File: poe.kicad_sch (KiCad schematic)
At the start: 85 parts

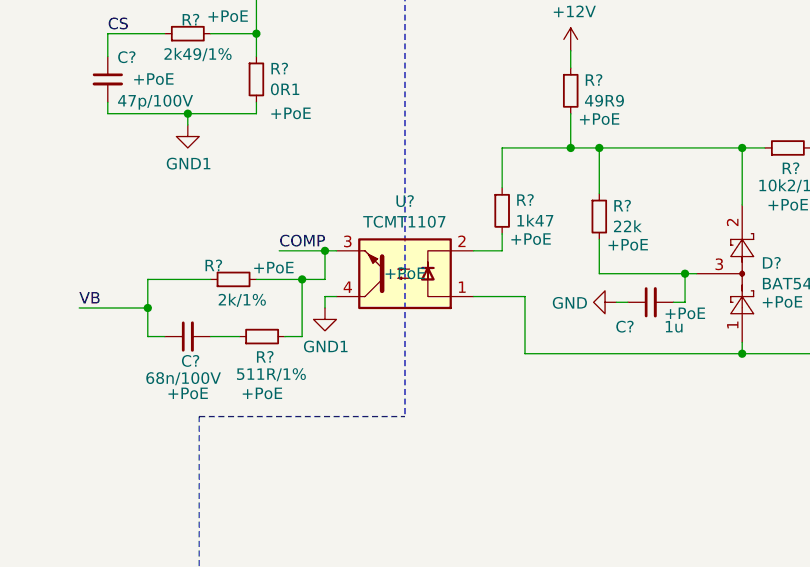
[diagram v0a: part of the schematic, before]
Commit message: poe.kicad_sch: Flip the optocoupler
Signed-off-by: Dominik Sliwa <dominik@sliwa.io>
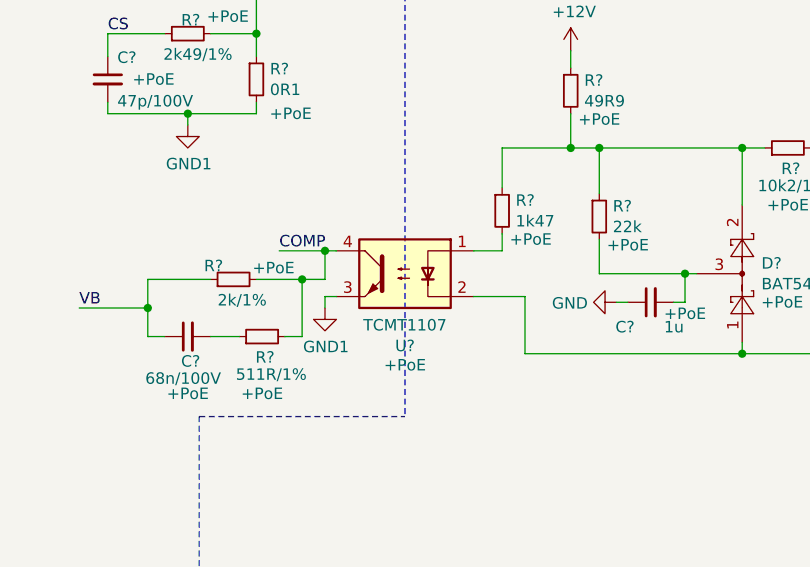
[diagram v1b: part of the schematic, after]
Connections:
- net COMP: now also U?.4; no longer U?.3
- net GND1: now also U?.3; no longer U?.4
- net at C?.2, D?.1, R?.2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: now also U?.2; no longer U?.1
- net at R?.2: now also U?.1; no longer U?.2
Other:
- moved on the sheet: U?
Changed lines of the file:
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@@
   (junction (at 274.32 35.56) (diameter 0.9144) (color 0 0 0 0))
   (junction (at 281.94 139.065) (diameter 0.9144) (color 0 0 0 0))
+  (no_connect (at 113.03 129.54))
+  (no_connect (at 72.39 157.48))
   (no_connect (at 72.39 129.54))
   (no_connect (at 72.39 154.94))
-  (no_connect (at 72.39 157.48))
-  (no_connect (at 113.03 129.54))
   (bus_entry (at 33.02 33.02) (size 2.54 2.54)
     (stroke (width 0.1524) (type solid) (color 0 0 0 0))
@@
     (property "Config" "+PoE" (id 4) (at 241.3 152.4 90))
   )
-  (symbol (lib_id "Isolator:TCMT1107") (at 199.39 149.225 180) (unit 1)
-    (in_bom yes) (on_board yes)
-    (property "Reference" "U?" (id 0) (at 199.39 141.2048 0))
-    (property "Value" "TCMT1107" (id 1) (at 199.39 143.5035 0))
-    (property "Footprint" "Package_SO:SOP-4_4.4x2.6mm_P1.27mm" (id 2) (at 199.39 141.605 0)
-      (effects (font (size 1.27 1.27)) hide)
-    )
-    (property "Datasheet" "http://www.vishay.com/docs/83510/tcmt1100.pdf" (id 3) (at 199.39 147.955 0)
+  (symbol (lib_id "Isolator:TCMT1107") (at 199.39 149.225 0) (mirror y) (unit 1)
+    (in_bom yes) (on_board yes)
+    (property "Reference" "U?" (id 0) (at 199.39 157.2452 0))
+    (property "Value" "TCMT1107" (id 1) (at 199.39 154.9465 0))
+    (property "Footprint" "Package_SO:SOP-4_4.4x2.6mm_P1.27mm" (id 2) (at 199.39 156.845 0)
+      (effects (font (size 1.27 1.27)) hide)
+    )
+    (property "Datasheet" "http://www.vishay.com/docs/83510/tcmt1100.pdf" (id 3) (at 199.39 150.495 0)
       (effects (font (size 1.27 1.27)) (justify left) hide)
     )
-    (property "Config" "+PoE" (id 4) (at 199.39 149.225 0))
+    (property "Config" "+PoE" (id 4) (at 199.39 159.385 0))
   )
   (symbol (lib_id "LightBlue:Transformer_Wurth_749119550") (at 199.39 45.72 0) (unit 1)

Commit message: Annotate symbools and assign capacitor footprints
Signed-off-by: Stefan Agner <stefan@agner.ch>
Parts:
- C70, C71, C72, C73, C74, C75, C76, C77, C78, C79, C80, C81, C82, C83, C84, C85, C86: renamed from C?; footprint (none) -> Capacitor_SMD:C_0805_2012Metric
- C87, C88, C89, C90, C91: renamed from C?; footprint (none) -> Capacitor_SMD:C_0402_1005Metric
- C92, C93: renamed from C?; footprint (none) -> Capacitor_Tantalum_SMD:CP_EIA-7343-31_Kemet-D
- gave numbers to parts that had none: 61

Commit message: Standardize page settings/add page titles
Signed-off-by: Stefan Agner <stefan@agner.ch>
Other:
- company: (none) -> Nabu Casa
- title: (none) -> Power over Ethernet
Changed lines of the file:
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@@
 (kicad_sch (version 20201015) (generator eeschema)
   (paper "A4")
+  (title_block
+    (title "Power over Ethernet")
+    (date "2021-01-12")
+    (rev "0.1")
+    (company "Nabu Casa")
+    (comment 1 "www.nabucasa.com")
+    (comment 2 "Light Blue")
+  )
   (junction (at 38.735 109.22) (diameter 0.9144) (color 0 0 0 0))
   (junction (at 40.64 35.56) (diameter 0.9144) (color 0 0 0 0))

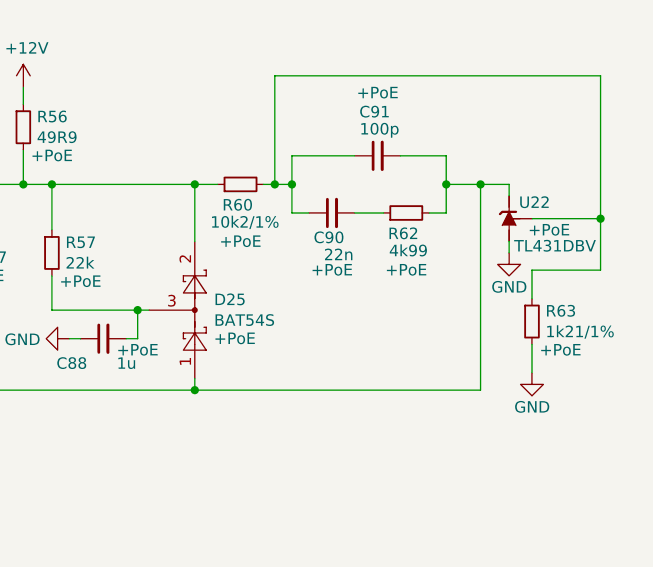
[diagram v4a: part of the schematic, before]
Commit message: Define more footprints and update Manufacturer/PartNumber fields
Signed-off-by: Stefan Agner <stefan@agner.ch>
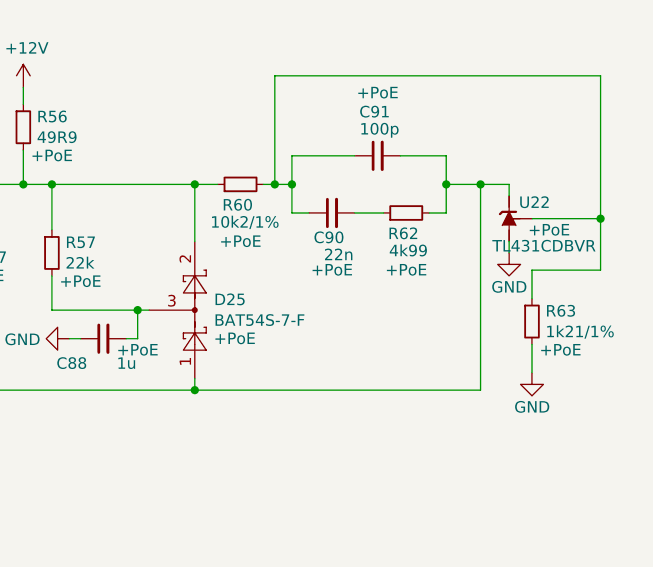
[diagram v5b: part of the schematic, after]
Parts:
- D10, D11, D12, D13, D14, D15, D16, D9: footprint (none) -> Diode_SMD:D_SMB; Manufacturer (none) -> Diodes Incorporated; PartNumber (none) -> B2100-13-F
- D17: footprint (none) -> Diode_SMD:D_SMB; Manufacturer (none) -> Diodes Incorporated; PartNumber (none) -> SMBJ58A-13-F
- D18, D24: footprint (none) -> Diode_SMD:D_SMC; Manufacturer (none) -> Diodes Incorporated; PartNumber (none) -> B3100-13-F
- D19, D20, D21, D22, D23, D26: footprint (none) -> Diode_SMD:D_SOD-123; Manufacturer (none) -> STMicroelectronics; PartNumber (none) -> BAT41ZFILM
- D25: value BAT54S -> BAT54S-7-F; Manufacturer (none) -> Diodes Incorporated; PartNumber (none) -> BAT54S-7-F
- D27: Manufacturer (none) -> Diodes Incorporated; PartNumber (none) -> BZX84C18-7-F
- Q4: Manufacturer (none) -> Nexperia USA; PartNumber (none) -> BCX56-16,115
- T1: Config (none) -> +PoE; Manufacturer (none) -> Würth Elektronik; PartNumber (none) -> 749119550
- U20: Manufacturer (none) -> Texas Instruments; PartNumber (none) -> TPS23734RMTR
- U21: Manufacturer (none) -> Vishay Semiconductor Opto Division; PartNumber (none) -> TCMT1107
- U22: value TL431DBV -> TL431CDBVR; Manufacturer (none) -> Texas Instruments; PartNumber (none) -> TL431CDBVR

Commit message: Add TPS23734 footprint
Add footprint for PoE controller TI TPS23734. Also fix/readd
Manufacturer which somehow got lost when opening.

Signed-off-by: Stefan Agner <stefan@agner.ch>
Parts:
- U20: footprint (none) -> LightBlue:Texas_VQFN-47-2EP_5x7mm_P0.4mm_ThermalVias

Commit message: Define footprint for remaining parts
- Fix footprint for 02x05 pin header
- Add footprint for Bourns SDR1006 Inductor (PoE)
- Define footprints for inductors
- Define footprints for ferrite beads
- Define footprint for fuse
- Define footprints for all resistors
- Define footprints for SD card and other components
- Switch ON Semi NCP114MX with TI TLV73333PDBV

Signed-off-by: Stefan Agner <stefan@agner.ch>
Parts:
- C92: Manufacturer (none) -> KEMET; PartNumber (none) -> T491X107K025AT
- C93: Manufacturer (none) -> KEMET; PartNumber (none) -> T491D336K025AT
- FB2, FB3: footprint (none) -> Resistor_SMD:R_0805_2012Metric; Manufacturer (none) -> Würth Elektronik; PartNumber (none) -> 742792031
- L3: footprint (none) -> Inductor_SMD:L_Bourns_SRN6045TA; Manufacturer (none) -> Bourns; PartNumber (none) -> SRN6045TA-3R3Y
- L4: footprint (none) -> LightBlue:L_Bourns-SDR1006; Manufacturer (none) -> Bourns; PartNumber (none) -> SDR1006-222KL
- L5: footprint (none) -> Inductor_SMD:L_Bourns_SRR1260; Manufacturer (none) -> Bourns; PartNumber (none) -> SRR1260-100M
- Q1: Manufacturer (none) -> ON Semiconductor; PartNumber (none) -> FDMC2523P
- Q2: Manufacturer (none) -> ON Semiconductor; PartNumber (none) -> FDMS86255
- Q3, Q5: Manufacturer (none) -> Texas Instruments; PartNumber (none) -> CSD17510Q5A
- R37, R38, R39, R40, R41, R42, R43, R44, R45, R46, R47, R48, R49, R50, R51, R52, R53, R54, R55, R56, R57, R58, R59, R60, R61, R62, R63: footprint (none) -> Resistor_SMD:R_0402_1005Metric

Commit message: Fix CM4 footprint, assign mounting holes/fiducials
Signed-off-by: Stefan Agner <stefan@agner.ch>
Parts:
- TP1: footprint (none) -> TestPoint:TestPoint_Pad_D2.0mm
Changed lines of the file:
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@@
     (property "Reference" "TP1" (id 0) (at 59.7535 132.9498 90))
     (property "Value" "TestPoint" (id 1) (at 59.7535 136.5185 90))
-    (property "Footprint" "" (id 2) (at 60.325 129.54 0)
+    (property "Footprint" "TestPoint:TestPoint_Pad_D2.0mm" (id 2) (at 60.325 129.54 0)
       (effects (font (size 1.27 1.27)) hide)
     )
